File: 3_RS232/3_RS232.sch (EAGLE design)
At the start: 8 parts, among them IC5 MAX211ECWI, X9 ALLSERIALD

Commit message: Add BOM
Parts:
- C40, C41, C44, C45, C48: OC_REICHELT (none) -> X7R-G0805 100N
- IC5: OC_FARNELL (none) -> 2519263
- X4: OC_REICHELT (none) -> D-SUB ST 09EU
- X9: OC_REICHELT (none) -> SL 2X10W 2,54
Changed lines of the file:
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@@
 <?xml version="1.0" encoding="utf-8"?>
 <!DOCTYPE eagle SYSTEM "eagle.dtd">
-<eagle version="7.7.0">
+<eagle version="7.6.0">
 <drawing>
 <settings>
@@
 </classes>
 <parts>
-<part name="C40" library="rcl" deviceset="C-EU" device="C0805" value="100n"/>
-<part name="C41" library="rcl" deviceset="C-EU" device="C0805" value="100n"/>
-<part name="C44" library="rcl" deviceset="C-EU" device="C0805" value="100n"/>
-<part name="C45" library="rcl" deviceset="C-EU" device="C0805" value="100n"/>
+<part name="C40" library="rcl" deviceset="C-EU" device="C0805" value="100n">
+<attribute name="OC_REICHELT" value="X7R-G0805 100N"/>
+</part>
+<part name="C41" library="rcl" deviceset="C-EU" device="C0805" value="100n">
+<attribute name="OC_REICHELT" value="X7R-G0805 100N"/>
+</part>
+<part name="C44" library="rcl" deviceset="C-EU" device="C0805" value="100n">
+<attribute name="OC_REICHELT" value="X7R-G0805 100N"/>
+</part>
+<part name="C45" library="rcl" deviceset="C-EU" device="C0805" value="100n">
+<attribute name="OC_REICHELT" value="X7R-G0805 100N"/>
+</part>
 <part name="FRAME2" library="frames" deviceset="A4L-LOC" device=""/>
-<part name="C48" library="rcl" deviceset="C-EU" device="C0805" value="100n"/>
-<part name="X4" library="con-subd" deviceset="M09HP" device=""/>
-<part name="IC5" library="maxim" deviceset="MAX211ECWI" device=""/>
-<part name="X9" library="AllSerial" deviceset="ALLSERIAL" device="D"/>
+<part name="C48" library="rcl" deviceset="C-EU" device="C0805" value="100n">
+<attribute name="OC_REICHELT" value="X7R-G0805 100N"/>
+</part>
+<part name="X4" library="con-subd" deviceset="M09HP" device="">
+<attribute name="OC_REICHELT" value="D-SUB ST 09EU"/>
+</part>
+<part name="IC5" library="maxim" deviceset="MAX211ECWI" device="">
+<attribute name="OC_FARNELL" value="2519263"/>
+</part>
+<part name="X9" library="AllSerial" deviceset="ALLSERIAL" device="D">
+<attribute name="OC_REICHELT" value="SL 2X10W 2,54"/>
+</part>
 <part name="GND1" library="supply1" deviceset="GND" device=""/>
 <part name="GND2" library="supply1" deviceset="GND" device=""/>
@@
 </plain>
 <instances>
-<instance part="C40" gate="G$1" x="93.98" y="116.84" rot="R90"/>
-<instance part="C41" gate="G$1" x="96.52" y="106.68" rot="R270"/>
-<instance part="C44" gate="G$1" x="142.24" y="114.3" rot="R180"/>
-<instance part="C45" gate="G$1" x="142.24" y="104.14" rot="R90"/>
+<instance part="C40" gate="G$1" x="93.98" y="116.84" rot="R90">
+<attribute name="OC_REICHELT" x="93.98" y="132.08" size="1.778" layer="96" display="off"/>
+</instance>
+<instance part="C41" gate="G$1" x="96.52" y="106.68" rot="R270">
+<attribute name="OC_REICHELT" x="96.52" y="106.68" size="1.778" layer="96"/>
+</instance>
+<instance part="C44" gate="G$1" x="142.24" y="114.3" rot="R180">
+<attribute name="OC_REICHELT" x="142.24" y="114.3" size="1.778" layer="96"/>
+</instance>
+<instance part="C45" gate="G$1" x="142.24" y="104.14" rot="R90">
+<attribute name="OC_REICHELT" x="142.24" y="104.14" size="1.778" layer="96"/>
+</instance>
 <instance part="FRAME2" gate="G$1" x="0" y="0"/>
-<instance part="C48" gate="G$1" x="71.12" y="142.24"/>
-<instance part="X4" gate="G$1" x="187.96" y="76.2" rot="R90"/>
+<instance part="C48" gate="G$1" x="71.12" y="142.24">
+<attribute name="OC_REICHELT" x="71.12" y="142.24" size="1.778" layer="96" display="off"/>
+</instance>
+<instance part="X4" gate="G$1" x="187.96" y="76.2" rot="R90">
+<attribute name="OC_REICHELT" x="187.96" y="76.2" size="1.778" layer="96" rot="R90" display="off"/>
+</instance>
 <instance part="IC5" gate="G$1" x="121.92" y="93.98"/>
 <instance part="IC5" gate="P" x="60.96" y="139.7"/>
-<instance part="X9" gate="DAT" x="45.72" y="81.28"/>
+<instance part="X9" gate="DAT" x="45.72" y="81.28">
+<attribute name="OC_REICHELT" x="45.72" y="81.28" size="1.778" layer="96" display="off"/>
+</instance>
 <instance part="X9" gate="PWR" x="30.48" y="139.7"/>
 <instance part="GND1" gate="1" x="30.48" y="119.38"/>

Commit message: add author
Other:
- note added: "Seegel Systeme Königstraße 57 90762 Fürth www.seegel-systeme.de post@seegel-systeme.de +49 (911) / 8915295"
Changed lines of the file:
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@@
 <?xml version="1.0" encoding="utf-8"?>
 <!DOCTYPE eagle SYSTEM "eagle.dtd">
-<eagle version="7.6.0">
+<eagle version="7.7.0">
 <drawing>
 <settings>
@@
 <plain>
 <text x="218.44" y="20.32" size="1.778" layer="94">RS232</text>
+<text x="165.1" y="7.62" size="1.778" layer="94">Seegel Systeme
+Königstraße 57
+90762 Fürth
+www.seegel-systeme.de
+post@seegel-systeme.de
++49 (911) / 8915295</text>
 </plain>
 <instances>
@@
 </schematic>
 </drawing>
+<compatibility>
+<note version="6.3" minversion="6.2.2" severity="warning">
+Since Version 6.2.2 text objects can contain more than one line,
+which will not be processed correctly with this version.
+</note>
+</compatibility>
 </eagle>

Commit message: final design & order
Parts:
- removed X9: ALLSERIALD, AllSerial:ALLSERIALD
- added X1: ALLSERIALSLAVE, AllSerialv2:ALLSERIALSLAVE
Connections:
- net +5V: now also X1SUP.+5V, X1SUP.VIN; no longer X9PWR.+5V, X9PWR.VIN
- net GND: now also X1SUP.GND; no longer X9PWR.GND
- net N$100: now also X1DATA.DSR; no longer X9DAT.DSR
- net N$93: now also X1DATA.TXD; no longer X9DAT.TXD
- net N$94: now also X1DATA.RXD; no longer X9DAT.RXD
- net N$95: now also X1DATA.CTS; no longer X9DAT.CTS
- net N$96: now also X1DATA.RTS; no longer X9DAT.RTS
- net N$97: now also X1DATA.DCD; no longer X9DAT.DCD
- net N$98: now also X1DATA.RI; no longer X9DAT.RI
- net N$99: now also X1DATA.DTR; no longer X9DAT.DTR
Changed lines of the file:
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@@
 <?xml version="1.0" encoding="utf-8"?>
 <!DOCTYPE eagle SYSTEM "eagle.dtd">
-<eagle version="7.7.0">
+<eagle version="7.6.0">
 <drawing>
 <settings>
@@
 <attribute name="OC_FARNELL" value="2519263"/>
 </part>
-<part name="X9" library="AllSerial" deviceset="ALLSERIAL" device="D">
-<attribute name="OC_REICHELT" value="SL 2X10W 2,54"/>
-</part>
 <part name="GND1" library="supply1" deviceset="GND" device=""/>
 <part name="GND2" library="supply1" deviceset="GND" device=""/>
@@
 <part name="P+2" library="supply1" deviceset="+5V" device=""/>
 <part name="P+3" library="supply1" deviceset="+5V" device=""/>
+<part name="X1" library="AllSerialv2" deviceset="ALLSERIALSLAVE" device=""/>
 </parts>
 <sheets>
@@
 <instance part="IC5" gate="G$1" x="121.92" y="93.98"/>
 <instance part="IC5" gate="P" x="60.96" y="139.7"/>
-<instance part="X9" gate="DAT" x="45.72" y="81.28">
-<attribute name="OC_REICHELT" x="45.72" y="81.28" size="1.778" layer="96" display="off"/>
-</instance>
-<instance part="X9" gate="PWR" x="30.48" y="139.7"/>
 <instance part="GND1" gate="1" x="30.48" y="119.38"/>
 <instance part="GND2" gate="1" x="104.14" y="63.5"/>
@@
 <instance part="P+2" gate="1" x="66.04" y="157.48"/>
 <instance part="P+3" gate="1" x="43.18" y="157.48"/>
+<instance part="X1" gate="DATA" x="45.72" y="81.28"/>
+<instance part="X1" gate="SUP" x="30.48" y="139.7"/>
 </instances>
 <busses>
@@
 <net name="N$93" class="0">
 <segment>
-<pinref part="X9" gate="DAT" pin="TXD"/>
 <pinref part="IC5" gate="G$1" pin="T1IN"/>
 <wire x1="55.88" y1="96.52" x2="106.68" y2="96.52" width="0.1524" layer="91"/>
+<pinref part="X1" gate="DATA" pin="TXD"/>
 </segment>
 </net>
@@
 <wire x1="106.68" y1="76.2" x2="76.2" y2="76.2" width="0.1524" layer="91"/>
 <wire x1="76.2" y1="76.2" x2="76.2" y2="93.98" width="0.1524" layer="91"/>
-<pinref part="X9" gate="DAT" pin="RXD"/>
 <wire x1="76.2" y1="93.98" x2="55.88" y2="93.98" width="0.1524" layer="91"/>
+<pinref part="X1" gate="DATA" pin="RXD"/>
 </segment>
 </net>
@@
 <wire x1="106.68" y1="91.44" x2="88.9" y2="91.44" width="0.1524" layer="91"/>
 <wire x1="88.9" y1="91.44" x2="88.9" y2="88.9" width="0.1524" layer="91"/>
-<pinref part="X9" gate="DAT" pin="CTS"/>
 <wire x1="88.9" y1="88.9" x2="55.88" y2="88.9" width="0.1524" layer="91"/>
+<pinref part="X1" gate="DATA" pin="CTS"/>
 </segment>
 </net>
@@
 <wire x1="106.68" y1="83.82" x2="86.36" y2="83.82" width="0.1524" layer="91"/>
 <wire x1="86.36" y1="83.82" x2="86.36" y2="91.44" width="0.1524" layer="91"/>
-<pinref part="X9" gate="DAT" pin="RTS"/>
 <wire x1="86.36" y1="91.44" x2="55.88" y2="91.44" width="0.1524" layer="91"/>
+<pinref part="X1" gate="DATA" pin="RTS"/>
 </segment>
 </net>
@@
 <wire x1="106.68" y1="78.74" x2="73.66" y2="78.74" width="0.1524" layer="91"/>
 <wire x1="73.66" y1="78.74" x2="73.66" y2="81.28" width="0.1524" layer="91"/>
-<pinref part="X9" gate="DAT" pin="DCD"/>
 <wire x1="73.66" y1="81.28" x2="55.88" y2="81.28" width="0.1524" layer="91"/>
+<pinref part="X1" gate="DATA" pin="DCD"/>
 </segment>
 </net>
@@
 <wire x1="106.68" y1="73.66" x2="71.12" y2="73.66" width="0.1524" layer="91"/>
 <wire x1="71.12" y1="73.66" x2="71.12" y2="78.74" width="0.1524" layer="91"/>
-<pinref part="X9" gate="DAT" pin="RI"/>
 <wire x1="71.12" y1="78.74" x2="55.88" y2="78.74" width="0.1524" layer="91"/>
+<pinref part="X1" gate="DATA" pin="RI"/>
 </segment>
 </net>
@@
 <wire x1="83.82" y1="81.28" x2="83.82" y2="86.36" width="0.1524" layer="91"/>
 <wire x1="83.82" y1="86.36" x2="55.88" y2="86.36" width="0.1524" layer="91"/>
-<pinref part="X9" gate="DAT" pin="DTR"/>
+<pinref part="X1" gate="DATA" pin="DTR"/>
 </segment>
 </net>
@@
 <wire x1="106.68" y1="93.98" x2="78.74" y2="93.98" width="0.1524" layer="91"/>
 <wire x1="78.74" y1="93.98" x2="78.74" y2="83.82" width="0.1524" layer="91"/>
-<pinref part="X9" gate="DAT" pin="DSR"/>
 <wire x1="78.74" y1="83.82" x2="55.88" y2="83.82" width="0.1524" layer="91"/>
+<pinref part="X1" gate="DATA" pin="DSR"/>
 </segment>
 </net>
 <net name="GND" class="0">
 <segment>
-<pinref part="X9" gate="PWR" pin="GND"/>
 <wire x1="30.48" y1="121.92" x2="30.48" y2="124.46" width="0.1524" layer="91"/>
 <pinref part="GND1" gate="1" pin="GND"/>
+<pinref part="X1" gate="SUP" pin="GND"/>
 </segment>
 <segment>
@@
 </segment>
 <segment>
-<pinref part="X9" gate="PWR" pin="VIN"/>
 <wire x1="40.64" y1="149.86" x2="43.18" y2="149.86" width="0.1524" layer="91"/>
 <wire x1="43.18" y1="149.86" x2="43.18" y2="154.94" width="0.1524" layer="91"/>
-<pinref part="X9" gate="PWR" pin="+5V"/>
 <wire x1="40.64" y1="142.24" x2="43.18" y2="142.24" width="0.1524" layer="91"/>
 <wire x1="43.18" y1="142.24" x2="43.18" y2="149.86" width="0.1524" layer="91"/>
 <junction x="43.18" y="149.86"/>
 <pinref part="P+3" gate="1" pin="+5V"/>
-</segment>
-</net>
+<pinref part="X1" gate="SUP" pin="+5V"/>
+<pinref part="X1" gate="SUP" pin="VIN"/>
+</segment>
+</net>

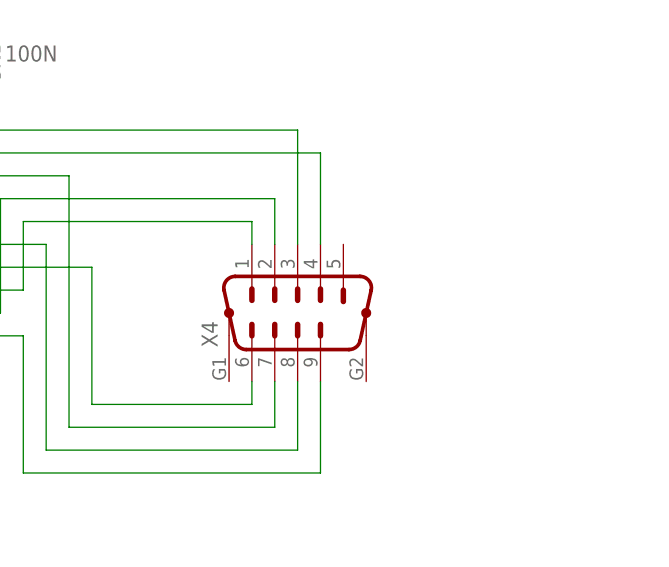
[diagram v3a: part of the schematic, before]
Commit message: fix GND connection
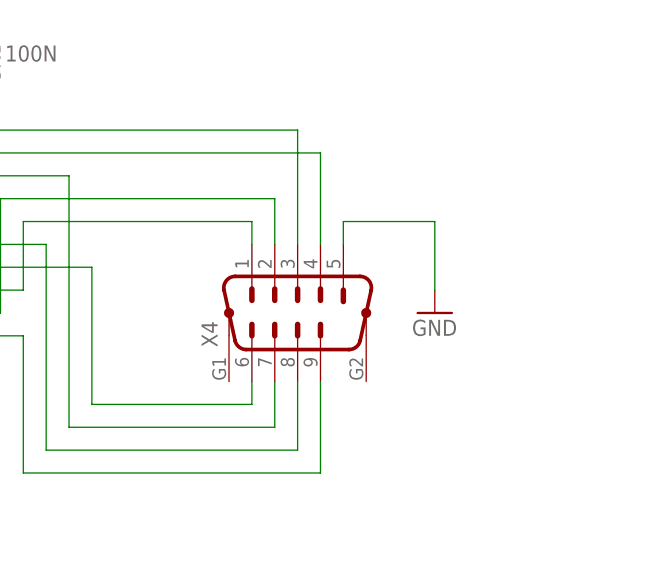
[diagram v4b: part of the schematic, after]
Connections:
- net GND: now also X4.5
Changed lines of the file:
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@@
 <?xml version="1.0" encoding="utf-8"?>
 <!DOCTYPE eagle SYSTEM "eagle.dtd">
-<eagle version="7.6.0">
+<eagle version="7.7.0">
 <drawing>
 <settings>
@@
 <part name="P+3" library="supply1" deviceset="+5V" device=""/>
 <part name="X1" library="AllSerialv2" deviceset="ALLSERIALSLAVE" device=""/>
+<part name="GND6" library="supply1" deviceset="GND" device=""/>
 </parts>
 <sheets>
@@
 <instance part="X1" gate="DATA" x="45.72" y="81.28"/>
 <instance part="X1" gate="SUP" x="30.48" y="139.7"/>
+<instance part="GND6" gate="1" x="203.2" y="76.2"/>
 </instances>
 <busses>
@@
 <pinref part="GND5" gate="1" pin="GND"/>
 </segment>
-</net>
+<segment>
+<pinref part="X4" gate="G$1" pin="5"/>
+<wire x1="193.04" y1="83.82" x2="193.04" y2="86.36" width="0.1524" layer="91"/>
+<pinref part="GND6" gate="1" pin="GND"/>
+<wire x1="193.04" y1="86.36" x2="203.2" y2="86.36" width="0.1524" layer="91"/>
+<wire x1="203.2" y1="86.36" x2="203.2" y2="78.74" width="0.1524" layer="91"/>
+</segment>
+</net>
